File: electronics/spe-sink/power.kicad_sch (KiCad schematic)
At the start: 7 parts, among them U5 AP2112K-3.3, U6 INA180A3

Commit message: Building out PDoE filter/isolation, etc
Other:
- note added: "Diode"
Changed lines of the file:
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@@
+    (effects (font (size 1.27 1.27)) (justify left bottom))
+  )
+  (text "Diode" (at 149.86 59.69 0)
     (effects (font (size 1.27 1.27)) (justify left bottom))
   )

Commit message: PD function board schematic progress
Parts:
- added C28: 1n_X7R_1608M, Applidyne_Capacitor:CAPC1608X90N, symbol appli_capacitor:1n_X7R_1608M
- added D5: LED_RED_1608M, Applidyne_LED:LEDC1608X80L40N, symbol appli_device:LED_RED_1608M
- added R27: R01_3216M, Applidyne_Resistor:RESC3216X60N, symbol appli_resistor:R01_3216M
- added R28: 1K00_1608M, Applidyne_Resistor:RESC1608X50N, symbol appli_resistor:1K00_1608M
- C18, C19: footprint CAPC2012* -> Applidyne_Capacitor:CAPC2012X110N
- C21: footprint CAPC1608* -> Applidyne_Capacitor:CAPC1608X90N
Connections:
- net GND: now also C28.2
- net I_SENSE: now also TEST2.1 (PAD), U6.1 (Vout), C28.1
- net at U6.3 (S+): now also R27.1
- net at U6.4 (S-): now also R27.2
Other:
- note added: "3.3V 10-bit ADC 2.5V = 3102 counts ~0.86mA resolution"
- note added: "PoDL Class 12 = 12.63W Regulated 5V @ 2.5A = 12.5W 2.5A across 10mOhm = 25mV Amplifier has 100x gain = 2.5V output"
- note removed: "TODO: Connect to MicroMod analog IO"
- note removed: "TODO: Size shunt for 1A peak loads?"

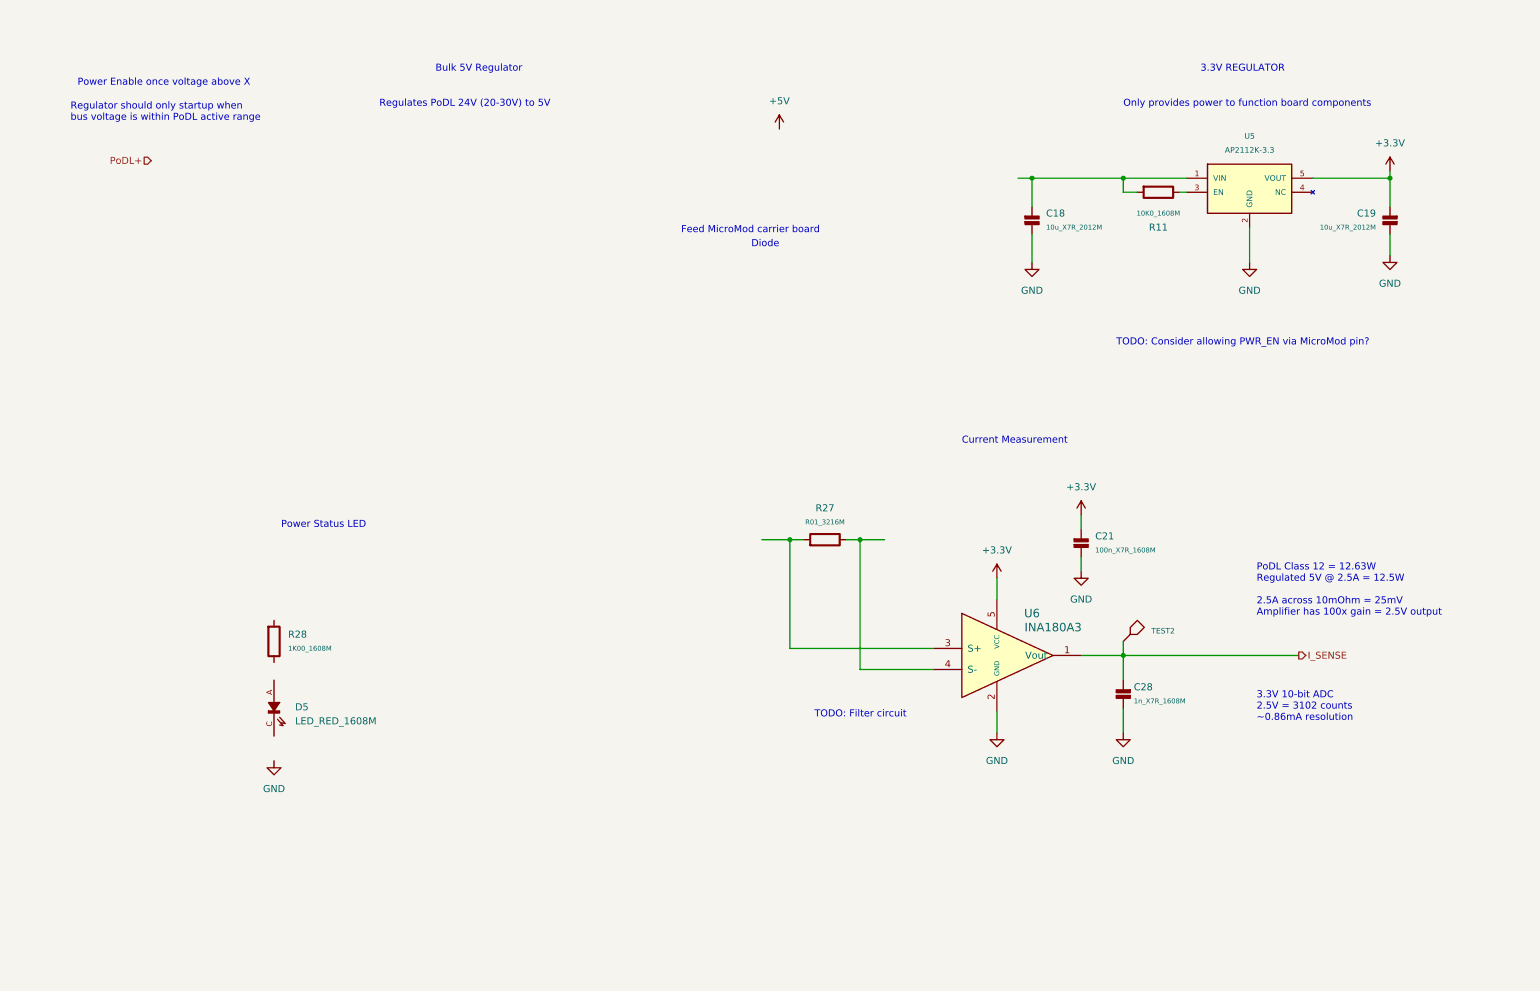
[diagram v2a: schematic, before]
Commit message: PD function board bulk regulator, cleanup, part placement
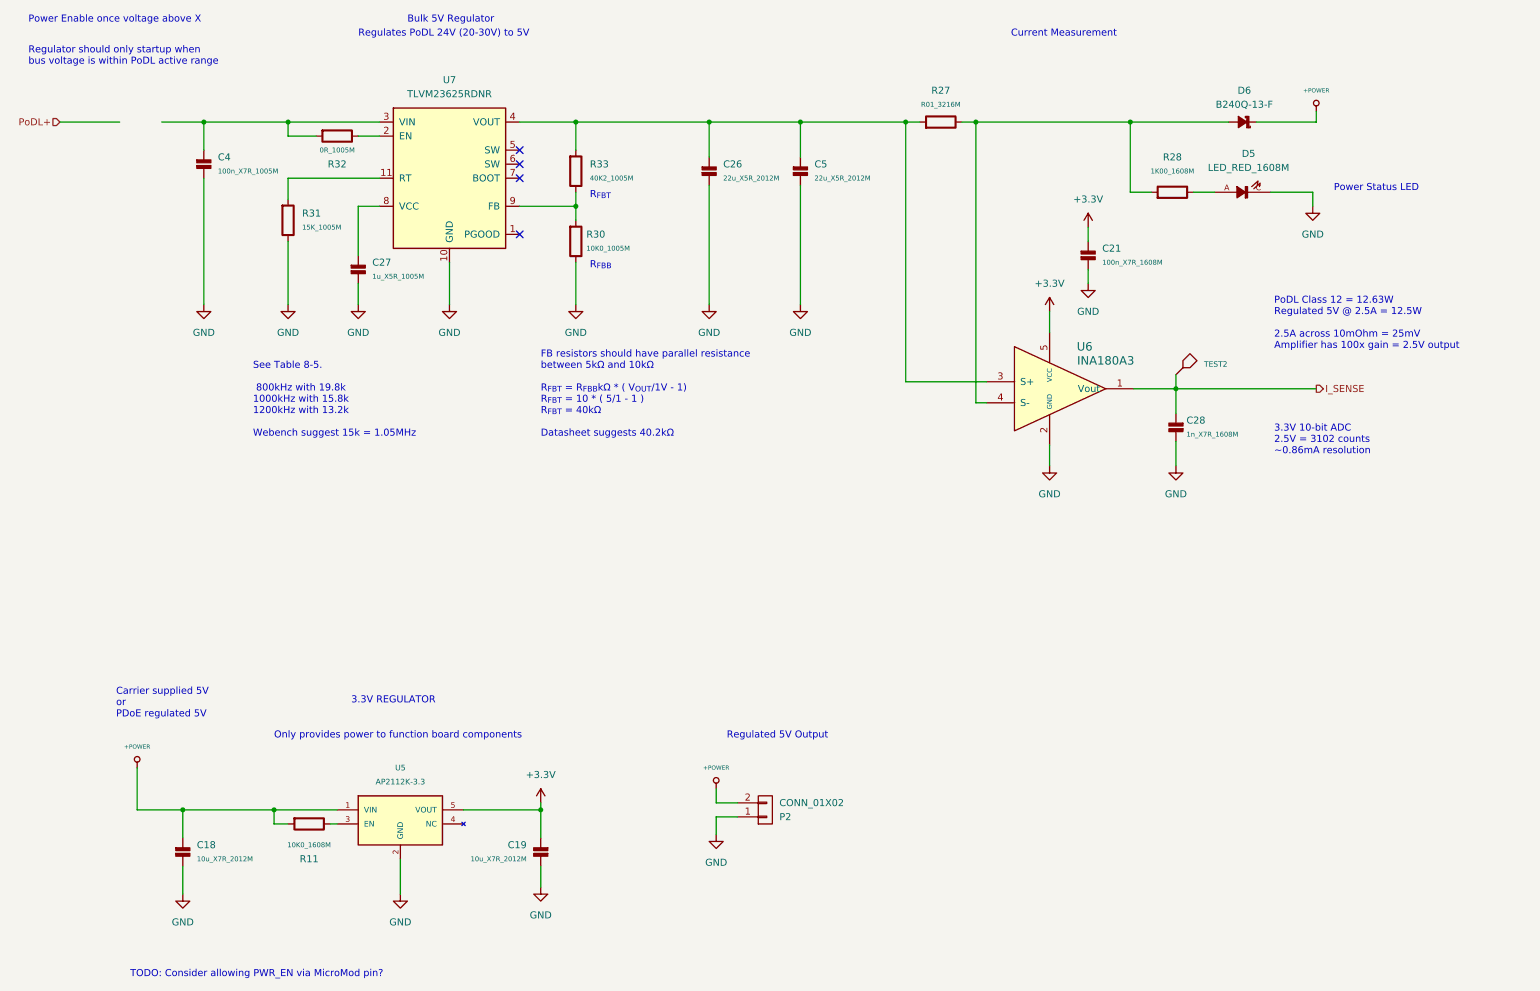
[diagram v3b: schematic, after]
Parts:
- added C26, C5: 22u_X5R_2012M, Applidyne_Capacitor:CAPC2012X110*, symbol appli_capacitor:22u_X5R_2012M
- added C27: 1u_X5R_1005M, Applidyne_Capacitor:CAPC1005X60N, symbol appli_capacitor:1u_X5R_1005M
- added C4: 100n_X7R_1005M, Applidyne_Capacitor:CAPC1005X60N, symbol appli_capacitor:100n_X7R_1005M
- added D6: B240Q-13-F, Applidyne_SOD:SODFL5436X262N, symbol appli_device:B240Q-13-F
- added P2: CONN_01X02, Applidyne_Connector_Wurth:61300211121, symbol appli_connector_wurth:CONN_01X02
- added R30: 10K0_1005M, Applidyne_Resistor:RESC1005X40N, symbol appli_resistor:10K0_1005M
- added R31: 15K_1005M, Applidyne_Resistor:RESC1005X40N, symbol appli_resistor:15K_1005M
- added R32: 0R_1005M, Applidyne_Resistor:RESC1005X40N, symbol appli_resistor:0R_1005M
- added R33: 40K2_1005M, Applidyne_Resistor:RESC1005X40N, symbol appli_resistor:40K2_1005M
- added U7: TLVM23625RDNR, Applidyne_QFN:QFN50P450X350X200-11-FCMOD11, symbol appli_regulator:TLVM23625RDNR
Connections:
- net GND: now also D5.C, C26.2, C27.2, C4.2, C5.2, P2.1 (P1), R30.2, R31.2, U7.10 (GND)
- net at R27.1, U6.3 (S+): now also C26.1, C5.1, R33.1, U7.4 (VOUT)
- net at R27.2, U6.4 (S-): now also R28.1, D6.A
- net at D5.A: now also R28.2
- net +POWER: now reaches C18.1, R11.1, U5.1 (VIN)
- net +POWER: now also D6.C, P2.2 (P2)
- new net: C4.1, R32.1, U7.3 (VIN)
- new net: R31.1, U7.11 (RT)
- new net: R30.1, R33.2, U7.9 (FB)
- new net: R32.2, U7.2 (EN)
- new net: C27.1, U7.8 (VCC)
- no-connect marks 0 -> 4
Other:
- note added: "Carrier supplied 5V or PDoE regulated 5V"
- note added: "FB resistors should have parallel resistance between 5kΩ and 10kΩ R_{FBT} = R_{FBB}kΩ * ( V_{OUT}/1V - 1) R_{FBT} = 10 * ( 5/1 - 1 ) R_{FBT} = 40kΩ Datasheet suggests 40.2kΩ"
- note added: "R_{FBB}"
- note added: "R_{FBT}"
- note added: "Regulated 5V Output"
- note added: "See Table 8-5. 800kHz with 19.8k 1000kHz with 15.8k 1200kHz with 13.2k Webench suggest 15k = 1.05MHz"
- note removed: "Diode"
- note removed: "Feed MicroMod carrier board"
- note removed: "TODO: Filter circuit"
- moved on the sheet: C18, C19, C21, C28, D5, R11, R27, R28, TEST2, U5, U6

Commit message: PD sink board routing, minor sch changes, etc
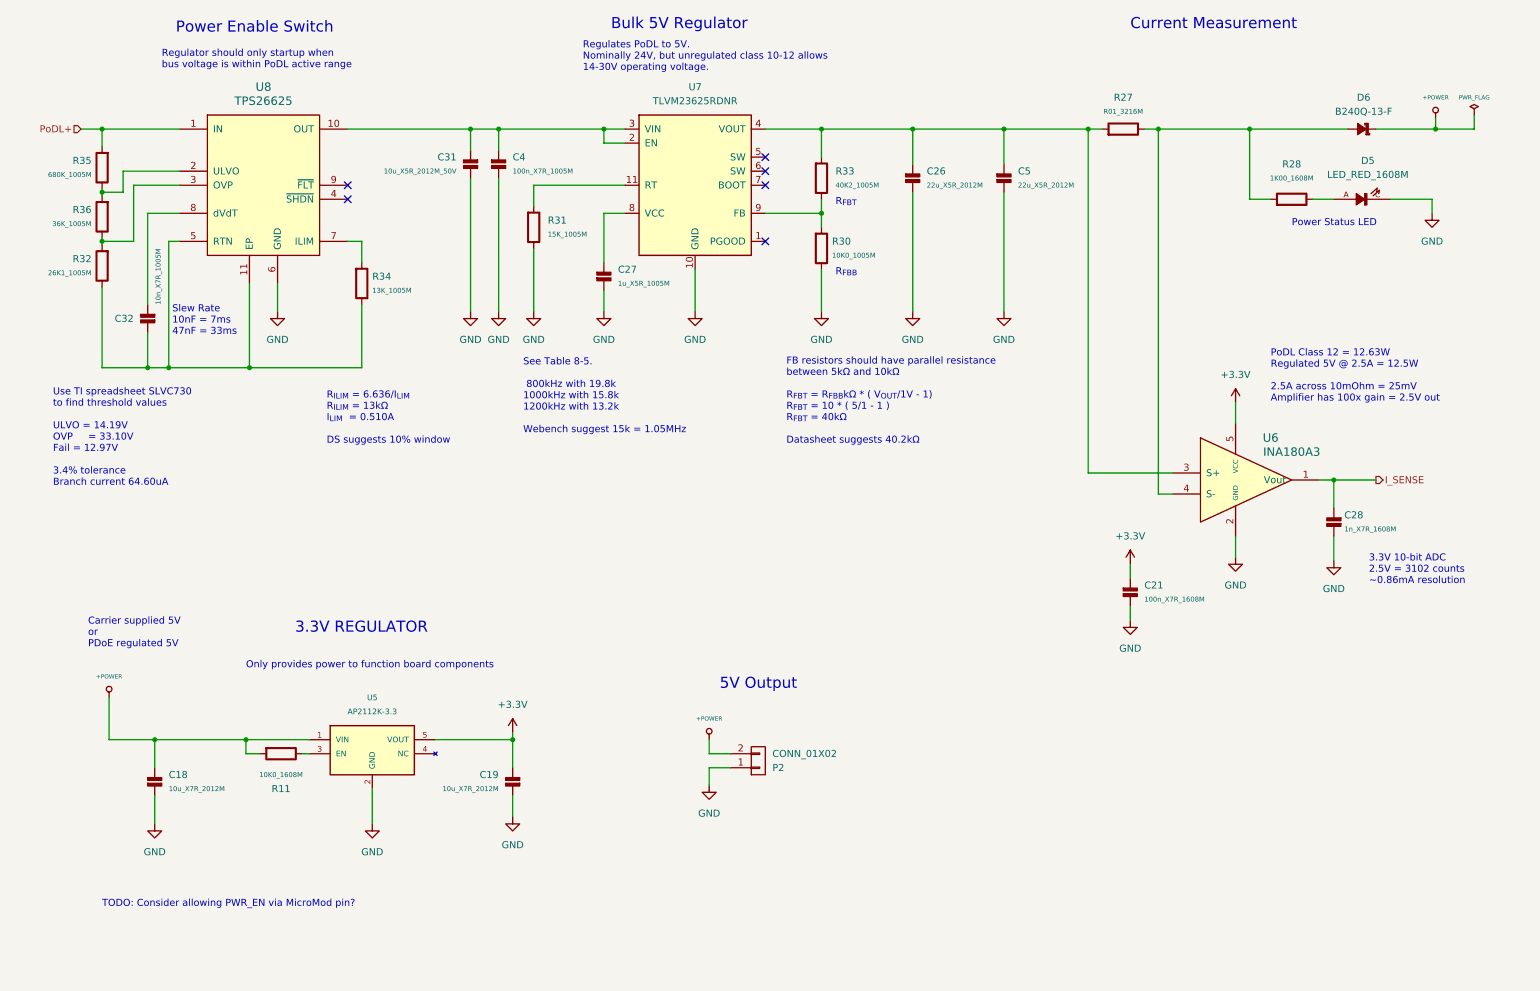
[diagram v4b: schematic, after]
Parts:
- removed R32: 0R_1005M, Applidyne_Resistor:RESC1005X40N, symbol appli_resistor:0R_1005M
- removed TEST2: CLIP_HOOK_BLUE, Applidyne_Test:KEYSTONE_5117, symbol appli_test_points:CLIP_HOOK_BLUE
- added C31: 10u_X5R_2012M_50V, Applidyne_Capacitor:CAPC2012X110N, symbol appli_capacitor:10u_X5R_2012M_50V
- added C32: 10n_X7R_1005M, Applidyne_Capacitor:CAPC1005X60N, symbol appli_capacitor:10n_X7R_1005M
- added R32: 26K1_1005M, Applidyne_Resistor:RESC1005X40N, symbol appli_resistor:26K1_1005M
- added R34: 13K_1005M, Applidyne_Resistor:RESC1005X40N, symbol appli_resistor:13K_1005M
- added R35: 680K_1005M, Applidyne_Resistor:RESC1005X40N, symbol appli_resistor:680K_1005M
- added R36: 36K_1005M, Applidyne_Resistor:RESC1005X40N, symbol appli_resistor:36K_1005M
- added U8: TPS26625, Applidyne_SON:SON50P300X300X90-11T240X165N_RELIEF, symbol appli_special:TPS26625
- C26, C5: footprint Applidyne_Capacitor:CAPC2012X110* -> Applidyne_Capacitor:CAPC2012X110N
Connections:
- net GND: now also C31.2, U8.6 (GND)
- net PoDL+: now also R35.1, U8.1 (IN)
- net at C4.1, U7.3 (VIN): now also U7.2 (EN), C31.1, U8.10 (OUT)
- new net: R32.1, R36.2, U8.3 (OVP)
- new net: C32.2, R32.2, R34.2, U8.11 (EP), U8.5 (RTN)
- new net: R35.2, R36.1, U8.2 (ULVO)
- new net: R34.1, U8.7 (ILIM)
- new net: C32.1, U8.8 (dVdT)
- no-connect marks 4 -> 6
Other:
- note added: "5V Output"
- note added: "PoDL Class 12 = 12.63W Regulated 5V @ 2.5A = 12.5W 2.5A across 10mOhm = 25mV Amplifier has 100x gain = 2.5V out"
- note added: "Power Enable Switch"
- note added: "R_{ILIM} = 6.636/I_{LIM} R_{ILIM} = 13kΩ I_{LIM} = 0.510A DS suggests 10% window"
- note added: "Regulates PoDL to 5V. Nominally 24V, but unregulated class 10-12 allows 14-30V operating voltage."
- note added: "Slew Rate 10nF = 7ms 47nF = 33ms"
- note added: "Use TI spreadsheet SLVC730 to find threshold values ULVO = 14.19V OVP = 33.10V Fail = 12.97V 3.4% tolerance Branch current 64.60uA"
- note removed: "PoDL Class 12 = 12.63W Regulated 5V @ 2.5A = 12.5W 2.5A across 10mOhm = 25mV Amplifier has 100x gain = 2.5V output"
- note removed: "Power Enable once voltage above X"
- note removed: "Regulated 5V Output"
- note removed: "Regulates PoDL 24V (20-30V) to 5V"
- moved on the sheet: C18, C19, C21, C26, C27, C28, C4, C5, D5, D6, P2, R11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
